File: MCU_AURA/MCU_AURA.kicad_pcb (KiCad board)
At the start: 4 copper layers, 50 x 50 mm, 111 parts, among them IC1 PCA9685PW,118, J1 TF-CARD_H1.8, J100 USB_C_Receptacle_USB2.0_16P, J200 TC2050-IDC-430, J400 532617004, J401 532617004, J402 532617004, J403 532617012, J404 532617007, J405 532617007, J406 532617012, J407 532617007, J408 532617004, Q300 BSS138, Q301 BSS138, Q302 BSS138, U100 TPS2115ADRBR, U101 TLV62566DBVR, U102 AP2127N-1.8, U200 ESP32-S3-WROOM-1, U201 USBLC6-2SC6, U300 ICM-20948, U301 BMP280

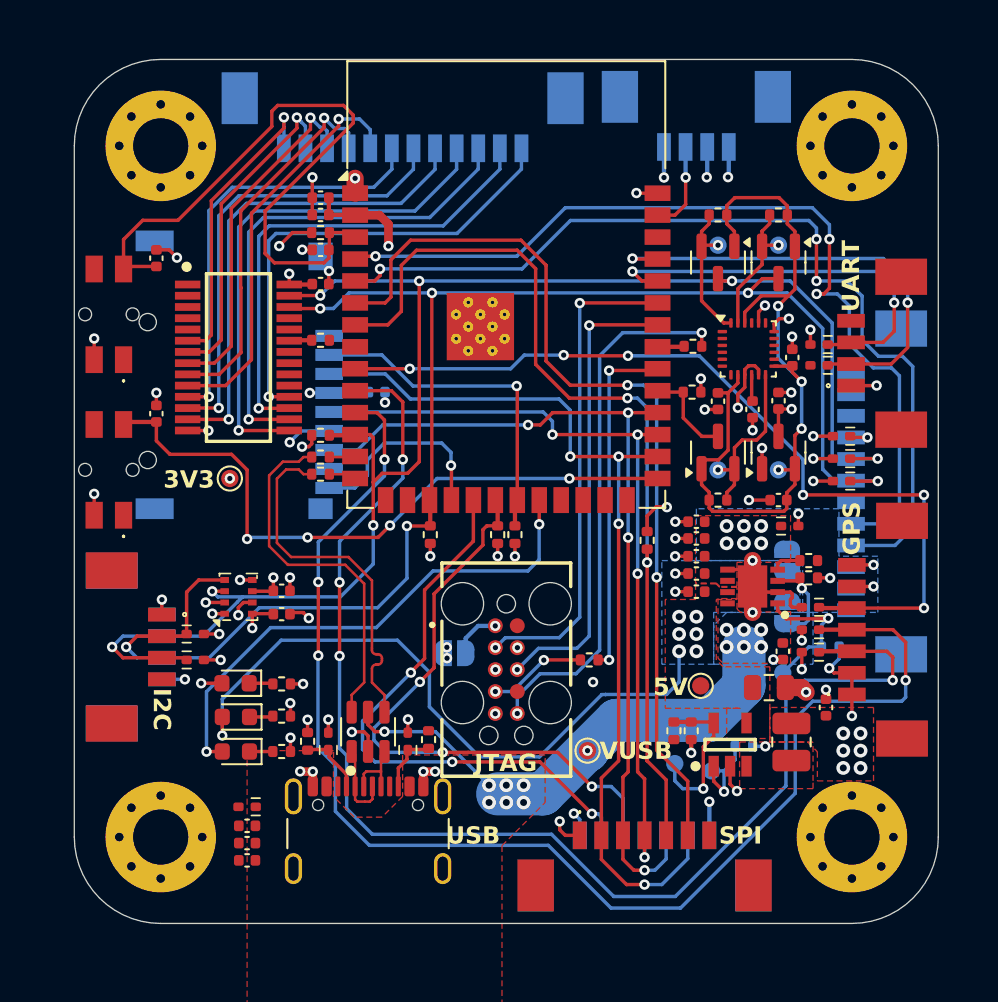
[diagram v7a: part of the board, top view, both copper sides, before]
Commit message: Replaced JTAG with Flash
JTAG is used through USB so a Flash chip was added to MCU. PDB is just being cleaned up currently.
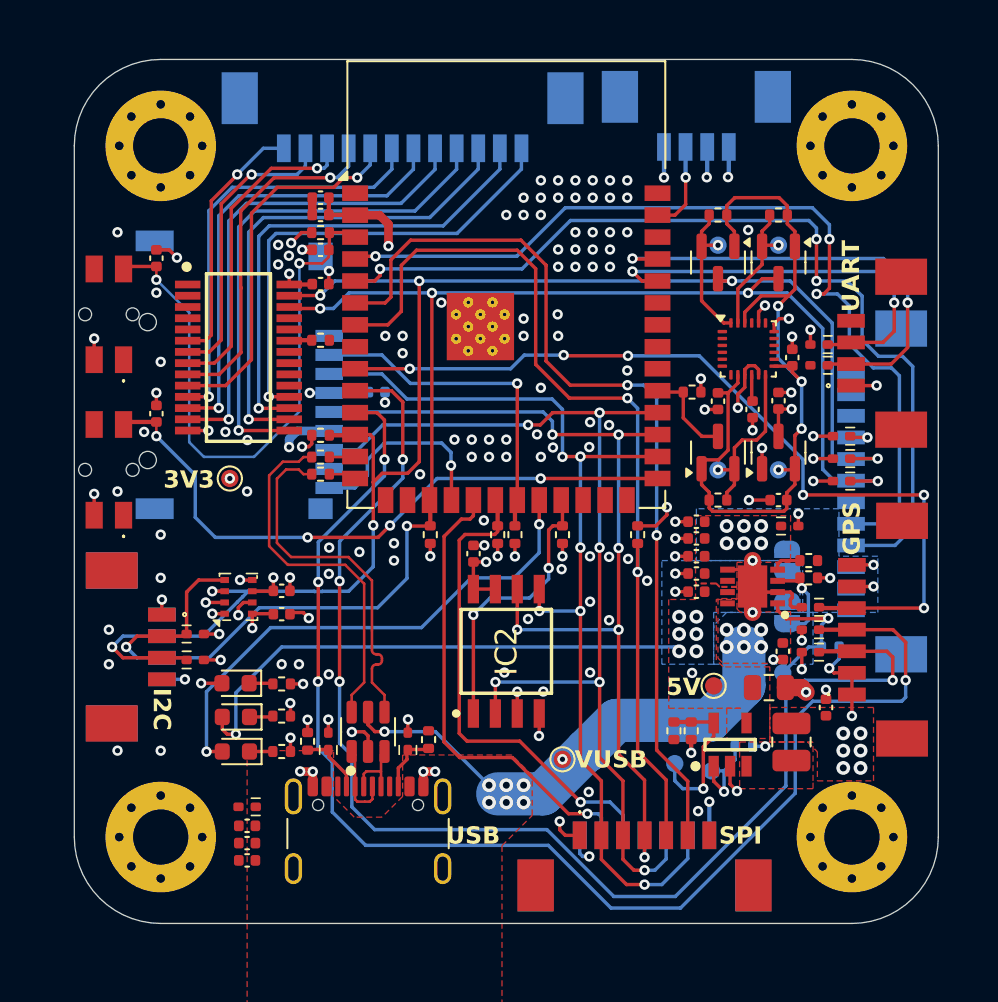
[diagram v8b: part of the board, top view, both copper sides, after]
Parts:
- removed J200: TC2050-IDC-430, TC2050-IDC:TC2050-IDC
- removed JP200: SolderJumper_2_Bridged, Jumper:SolderJumper-2_P1.3mm_Open_RoundedPad1.0x1.5mm
- removed R2: 22R, Resistor_SMD:R_0402_1005Metric
- added C1: 100n, Capacitor_SMD:C_0402_1005Metric, F.Cu at (123.1, 78.6)
- added IC2: W25Q128JVSIQ, W25Q128JVSIQ:SOIC127P790X216-8N, F.Cu at (125.0, 84.2)
- R1: value 22R -> 10k
- moved R1 7.41 mm to (128.2, 77.5), turned to -90 degrees
- moved TP100 1.53 mm to (128.2, 90.5)
- moved TP101 0.75 mm to (137.0, 86.2)
- moved R401 0.64 mm to (132.6, 77.5)
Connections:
- R1 pad 1: /200_ESP32/TCK_D -> FLASH_CS
- R1 pad 2: /200_ESP32/TCK -> +3V3
- U200 pad 23: unconnected-(U200-IO21-Pad23) -> FLASH_CS
- U200 pad 32: /200_ESP32/TCK_D -> unconnected-(U200-IO39-Pad32)
- U200 pad 33: /200_ESP32/TDO_D -> unconnected-(U200-IO40-Pad33)
- U200 pad 34: /200_ESP32/TDI -> unconnected-(U200-IO41-Pad34)
- U200 pad 35: /200_ESP32/TMS -> unconnected-(U200-IO42-Pad35)
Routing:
- net /200_ESP32/TDO: track 31.4 -> 0.00 mm, vias 2 -> 0
- net /200_ESP32/TMS: track 28.3 -> 0.00 mm, vias 2 -> 0
- net /200_ESP32/TDI: track 26.9 -> 0.00 mm, vias 2 -> 0
- net /200_ESP32/TCK_D: track 20.0 -> 0.00 mm, vias 2 -> 0
- net FLASH_CS: track 0.00 -> 16.2 mm, vias 0 -> 2
- net SCK: track 45.9 -> 54.6 mm, vias 4 -> 6
- net MISO: track 50.3 -> 58.6 mm, vias 4 -> 6
- net +5V_FILT: track 38.6 -> 30.9 mm
- net RF_CS: track 35.2 -> 28.1 mm, vias 3 -> 1
- net RF_RST: track 33.6 -> 27.0 mm, vias 3 -> 1
- net /200_ESP32/TCK: track 5.68 -> 0.00 mm, vias 2 -> 0
- net +3V3: track 47.6 -> 51.9 mm, vias 35 -> 36
- net /200_ESP32/EN: track 38.1 -> 34.2 mm, vias 0 -> 2
- net MOSI: track 53.9 -> 57.6 mm, vias 4 -> 6
- net SERVO_1: track 17.6 -> 14.7 mm
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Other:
- board text removed: "JTAG"
